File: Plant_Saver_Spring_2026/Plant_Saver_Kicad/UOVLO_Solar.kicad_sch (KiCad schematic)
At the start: 10 parts, among them Q10 G09P02L, Q11 SSF1341, U5 MCP6547T_I_MS

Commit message: Footprint correction
Changed the DHT20 from a header pin to the recommended SIP. Also had to reannotate in order to assign footprints.
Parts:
- renumbered Q11 to Q9, R34 to R38, R35 to R39, R36 to R40, R30 to R41, R31 to R42, R37 to R43, R38 to R44, U5 to U17
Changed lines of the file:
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@@
 		(dnp no)
 		(fields_autoplaced yes)
-		(property "Reference" "U5"
+		(property "Reference" "U17"
 			(at 158.75 71.12 0)
 			(effects
@@
 			(project ""
 				(path "/7f244634-d37a-4ff0-ba36-8027330ab1bd/c1b5c94f-5fb5-4e2b-895b-5d171c372d7d/9fa29de7-25a7-4316-bbea-8ab2651dedf4"
-					(reference "U5")
+					(reference "U17")
 					(unit 1)
 				)
@@
 		(dnp no)
 		(fields_autoplaced yes)
-		(property "Reference" "U5"
+		(property "Reference" "U17"
 			(at 158.75 91.44 0)
 			(effects
@@
 			(project ""
 				(path "/7f244634-d37a-4ff0-ba36-8027330ab1bd/c1b5c94f-5fb5-4e2b-895b-5d171c372d7d/9fa29de7-25a7-4316-bbea-8ab2651dedf4"
-					(reference "U5")
+					(reference "U17")
 					(unit 2)
 				)
@@
 		(dnp no)
 		(fields_autoplaced yes)
-		(property "Reference" "U5"
+		(property "Reference" "U17"
 			(at 104.14 120.65 90)
 			(effects
@@
 			(project ""
 				(path "/7f244634-d37a-4ff0-ba36-8027330ab1bd/c1b5c94f-5fb5-4e2b-895b-5d171c372d7d/9fa29de7-25a7-4316-bbea-8ab2651dedf4"
-					(reference "U5")
+					(reference "U17")
 					(unit 3)
 				)
@@
 		(dnp no)
 		(fields_autoplaced yes)
-		(property "Reference" "R35"
+		(property "Reference" "R39"
 			(at 116.84 91.4399 0)
 			(effects
@@
 			(project "Plant_Saver_Dev"
 				(path "/7f244634-d37a-4ff0-ba36-8027330ab1bd/c1b5c94f-5fb5-4e2b-895b-5d171c372d7d/9fa29de7-25a7-4316-bbea-8ab2651dedf4"
-					(reference "R35")
+					(reference "R39")
 					(unit 1)
 				)
@@
 		(dnp no)
 		(fields_autoplaced yes)
-		(property "Reference" "R30"
+		(property "Reference" "R41"
 			(at 140.97 83.8199 0)
 			(effects
@@
 			(project "Plant_Saver_Dev"
 				(path "/7f244634-d37a-4ff0-ba36-8027330ab1bd/c1b5c94f-5fb5-4e2b-895b-5d171c372d7d/9fa29de7-25a7-4316-bbea-8ab2651dedf4"
-					(reference "R30")
+					(reference "R41")
 					(unit 1)
 				)
@@
 		(dnp no)
 		(fields_autoplaced yes)
-		(property "Reference" "R38"
+		(property "Reference" "R44"
 			(at 203.2 74.93 90)
 			(effects
@@
 			(project "Plant_Saver_Dev"
 				(path "/7f244634-d37a-4ff0-ba36-8027330ab1bd/c1b5c94f-5fb5-4e2b-895b-5d171c372d7d/9fa29de7-25a7-4316-bbea-8ab2651dedf4"
-					(reference "R38")
+					(reference "R44")
 					(unit 1)
 				)
@@
 		(dnp no)
 		(fields_autoplaced yes)
-		(property "Reference" "#PWR022"
+		(property "Reference" "#PWR030"
 			(at 114.3 134.62 0)
 			(effects
@@
 			(project ""
 				(path "/7f244634-d37a-4ff0-ba36-8027330ab1bd/c1b5c94f-5fb5-4e2b-895b-5d171c372d7d/9fa29de7-25a7-4316-bbea-8ab2651dedf4"
-					(reference "#PWR022")
+					(reference "#PWR030")
 					(unit 1)
 				)
@@
 		(dnp no)
 		(fields_autoplaced yes)
-		(property "Reference" "R34"
+		(property "Reference" "R38"
 			(at 116.84 73.6599 0)
 			(effects
@@
 			(project "Plant_Saver_Dev"
 				(path "/7f244634-d37a-4ff0-ba36-8027330ab1bd/c1b5c94f-5fb5-4e2b-895b-5d171c372d7d/9fa29de7-25a7-4316-bbea-8ab2651dedf4"
-					(reference "R34")
+					(reference "R38")
 					(unit 1)
 				)
@@
 		(dnp no)
 		(fields_autoplaced yes)
-		(property "Reference" "R37"
+		(property "Reference" "R43"
 			(at 175.26 73.6599 0)
 			(effects
@@
 			(project "Plant_Saver_Dev"
 				(path "/7f244634-d37a-4ff0-ba36-8027330ab1bd/c1b5c94f-5fb5-4e2b-895b-5d171c372d7d/9fa29de7-25a7-4316-bbea-8ab2651dedf4"
-					(reference "R37")
+					(reference "R43")
 					(unit 1)
 				)
@@
 		(dnp no)
 		(fields_autoplaced yes)
-		(property "Reference" "R36"
+		(property "Reference" "R40"
 			(at 116.84 110.4899 0)
 			(effects
@@
 			(project "Plant_Saver_Dev"
 				(path "/7f244634-d37a-4ff0-ba36-8027330ab1bd/c1b5c94f-5fb5-4e2b-895b-5d171c372d7d/9fa29de7-25a7-4316-bbea-8ab2651dedf4"
-					(reference "R36")
+					(reference "R40")
 					(unit 1)
 				)
@@
 		(dnp no)
 		(fields_autoplaced yes)
-		(property "Reference" "#PWR023"
+		(property "Reference" "#PWR031"
 			(at 209.55 90.17 0)
 			(effects
@@
 			(project ""
 				(path "/7f244634-d37a-4ff0-ba36-8027330ab1bd/c1b5c94f-5fb5-4e2b-895b-5d171c372d7d/9fa29de7-25a7-4316-bbea-8ab2651dedf4"
-					(reference "#PWR023")
+					(reference "#PWR031")
 					(unit 1)
 				)
@@
 		(dnp no)
 		(fields_autoplaced yes)
-		(property "Reference" "R31"
+		(property "Reference" "R42"
 			(at 140.97 96.5199 0)
 			(effects
@@
 			(project "Plant_Saver_Dev"
 				(path "/7f244634-d37a-4ff0-ba36-8027330ab1bd/c1b5c94f-5fb5-4e2b-895b-5d171c372d7d/9fa29de7-25a7-4316-bbea-8ab2651dedf4"
-					(reference "R31")
+					(reference "R42")
 					(unit 1)
 				)
@@
 		(on_board yes)
 		(dnp no)
-		(property "Reference" "Q11"
+		(property "Reference" "Q9"
 			(at 201.93 91.44 90)
 			(effects
@@
 			(project "Plant_Saver_Dev"
 				(path "/7f244634-d37a-4ff0-ba36-8027330ab1bd/c1b5c94f-5fb5-4e2b-895b-5d171c372d7d/9fa29de7-25a7-4316-bbea-8ab2651dedf4"
-					(reference "Q11")
-					(unit 1)
-				)
+					(reference "Q9")
+					(unit 1)
+				)

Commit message: Charging updates and MicroSD started
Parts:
- R41: value 22.1K -> 205K
- R42: value 15K -> 301K
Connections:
- net GND: now also R38.2; no longer R40.2
- net Vcc: now also R40.1; no longer R38.1
- net at R39.1, U17.3 (+): now also R40.2; no longer R38.2
- net at R39.2, U17.6 (-): now also R38.1; no longer R40.1
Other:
- moved on the sheet: R38, R40
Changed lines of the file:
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@@
+	)
+	(junction
+		(at 114.3 78.74)
+		(diameter 0)
+		(color 0 0 0 0)
 	)
 	(junction
@@
 	(junction
 		(at 114.3 125.73)
-		(diameter 0)
-		(color 0 0 0 0)
-	)
-	(junction
-		(at 114.3 78.74)
 		(diameter 0)
 		(color 0 0 0 0)
@@
 			)
 		)
-		(property "Value" "22.1K"
+		(property "Value" "205K"
 			(at 140.97 86.3599 0)
 			(effects
@@
 	(symbol
 		(lib_id "Device:R_US")
-		(at 114.3 74.93 0)
+		(at 114.3 111.76 0)
 		(unit 1)
 		(exclude_from_sim no)
@@
 		(fields_autoplaced yes)
 		(property "Reference" "R38"
-			(at 116.84 73.6599 0)
+			(at 116.84 110.4899 0)
 			(effects
 				(font
@@
 		)
 		(property "Value" "402K"
-			(at 116.84 76.1999 0)
+			(at 116.84 113.0299 0)
 			(effects
 				(font
@@
 		)
 		(property "Footprint" "Resistor_THT:R_Axial_DIN0207_L6.3mm_D2.5mm_P10.16mm_Horizontal"
-			(at 115.316 75.184 90)
+			(at 115.316 112.014 90)
 			(effects
 				(font
@@
 		)
 		(property "Datasheet" "~"
-			(at 114.3 74.93 0)
+			(at 114.3 111.76 0)
 			(effects
 				(font
@@
 		)
 		(property "Description" "Resistor, US symbol"
-			(at 114.3 74.93 0)
+			(at 114.3 111.76 0)
 			(effects
 				(font
@@
 	(symbol
 		(lib_id "Device:R_US")
-		(at 114.3 111.76 0)
+		(at 114.3 74.93 0)
 		(unit 1)
 		(exclude_from_sim no)
@@
 		(fields_autoplaced yes)
 		(property "Reference" "R40"
-			(at 116.84 110.4899 0)
+			(at 116.84 73.6599 0)
 			(effects
 				(font
@@
 		)
 		(property "Value" "22.1K"
-			(at 116.84 113.0299 0)
+			(at 116.84 76.1999 0)
 			(effects
 				(font
@@
 		)
 		(property "Footprint" "Resistor_THT:R_Axial_DIN0207_L6.3mm_D2.5mm_P10.16mm_Horizontal"
-			(at 115.316 112.014 90)
+			(at 115.316 75.184 90)
 			(effects
 				(font
@@
 		)
 		(property "Datasheet" "~"
-			(at 114.3 111.76 0)
+			(at 114.3 74.93 0)
 			(effects
 				(font
@@
 		)
 		(property "Description" "Resistor, US symbol"
-			(at 114.3 111.76 0)
+			(at 114.3 74.93 0)
 			(effects
 				(font
@@
 			)
 		)
-		(property "Value" "15K"
+		(property "Value" "301K"
 			(at 140.97 99.0599 0)
 			(effects

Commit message: Misc. Charging Changes
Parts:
- removed Q9: SSF1341, Package_TO_SOT_SMD:SOT-23_Handsoldering, symbol Simulation_SPICE:PMOS
- added Q11: ISP12DP06NMXTSA1, ul_ISP12DP06NMXTSA1:PG-SOT223-4_INF, symbol Simulation_SPICE:PMOS
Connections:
- net Vin: now also Q11.3 (S)
- net at R43.2, U17.1, U17.7: now also Q11.2 (G)
- net at Q10.2 (G), R44.2: now also Q11.1 (D)
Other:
- note removed: "Double-Check This"
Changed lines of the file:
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@@
 	(generator_version "9.0")
 	(paper "A4")
-	(rectangle
-		(start 181.61 59.69)
-		(end 222.25 104.14)
-		(stroke
-			(width 0)
-			(type dash_dot)
-		)
-		(fill
-			(type none)
-		)
-	)
-	(text "Double-Check This"
-		(exclude_from_sim no)
-		(at 190.246 58.166 0)
-		(effects
-			(font
-				(size 1.27 1.27)
-			)
-		)
-	)
 	(text "Voltage window: 4.5 to 5.3 V"
 		(exclude_from_sim no)
-		(at 152.4 52.07 0)
+		(at 147.32 61.214 0)
 		(effects
 			(font
@@
 	)
 	(symbol
+		(lib_id "Simulation_SPICE:PMOS")
+		(at 193.04 91.44 0)
+		(unit 1)
+		(exclude_from_sim no)
+		(in_bom yes)
+		(on_board yes)
+		(dnp no)
+		(property "Reference" "Q11"
+			(at 201.93 91.44 90)
+			(effects
+				(font
+					(size 1.27 1.27)
+				)
+			)
+		)
+		(property "Value" "ISP12DP06NMXTSA1"
+			(at 199.39 91.44 90)
+			(effects
+				(font
+					(size 1.27 1.27)
+				)
+			)
+		)
+		(property "Footprint" "ul_ISP12DP06NMXTSA1:PG-SOT223-4_INF"
+			(at 198.12 88.9 0)
+			(effects
+				(font
+					(size 1.27 1.27)
+				)
+				(hide yes)
+			)
+		)
+		(property "Datasheet" ""
+			(at 193.04 104.14 0)
+			(effects
+				(font
+					(size 1.27 1.27)
+				)
+				(hide yes)
+			)
+		)
+		(property "Description" "P-MOSFET transistor, drain/source/gate"
+			(at 193.04 91.44 0)
+			(effects
+				(font
+					(size 1.27 1.27)
+				)
+				(hide yes)
+			)
+		)
+		(property "Sim.Device" "PMOS"
+			(at 193.04 108.585 0)
+			(effects
+				(font
+					(size 1.27 1.27)
+				)
+				(hide yes)
+			)
+		)
+		(property "Sim.Type" "VDMOS"
+			(at 193.04 110.49 0)
+			(effects
+				(font
+					(size 1.27 1.27)
+				)
+				(hide yes)
+			)
+		)
+		(property "Sim.Pins" "1=D 2=G 3=S"
+			(at 193.04 106.68 0)
+			(effects
+				(font
+					(size 1.27 1.27)
+				)
+				(hide yes)
+			)
+		)
+		(pin "1"
+		)
+		(pin "2"
+		)
+		(pin "3"
+		)
+		(instances
+			(project "Plant_Saver_Kicad"
+				(path "/7f244634-d37a-4ff0-ba36-8027330ab1bd/c1b5c94f-5fb5-4e2b-895b-5d171c372d7d/9fa29de7-25a7-4316-bbea-8ab2651dedf4"
+					(reference "Q11")
+					(unit 1)
+				)
+			)
+		)
+	)
+	(symbol
 		(lib_id "power:GND")
 		(at 209.55 83.82 0)
@@
 					(unit 1)
 				)
-			)
-		)
-	)
-	(symbol
-		(lib_id "Simulation_SPICE:PMOS")
-		(at 193.04 91.44 0)
-		(unit 1)
-		(exclude_from_sim no)
-		(in_bom yes)
-		(on_board yes)
-		(dnp no)
-		(property "Reference" "Q9"
-			(at 201.93 91.44 90)
-			(effects
-				(font
-					(size 1.27 1.27)
-				)
-			)
-		)
-		(property "Value" "SSF1341"
-			(at 199.39 91.44 90)
-			(effects
-				(font
-					(size 1.27 1.27)
-				)
-			)
-		)
-		(property "Footprint" "Package_TO_SOT_SMD:SOT-23_Handsoldering"
-			(at 198.12 88.9 0)
-			(effects
-				(font
-					(size 1.27 1.27)
-				)
-				(hide yes)
-			)
-		)
-		(property "Datasheet" "https://ngspice.sourceforge.io/docs/ngspice-html-manual/manual.xhtml#cha_MOSFETs"
-			(at 193.04 104.14 0)
-			(effects
-				(font
-					(size 1.27 1.27)
-				)
-				(hide yes)
-			)
-		)
-		(property "Description" "P-MOSFET transistor, drain/source/gate"
-			(at 193.04 91.44 0)
-			(effects
-				(font
-					(size 1.27 1.27)
-				)
-				(hide yes)
-			)
-		)
-		(property "Sim.Device" "PMOS"
-			(at 193.04 108.585 0)
-			(effects
-				(font
-					(size 1.27 1.27)
-				)
-				(hide yes)
-			)
-		)
-		(property "Sim.Type" "VDMOS"
-			(at 193.04 110.49 0)
-			(effects
-				(font
-					(size 1.27 1.27)
-				)
-				(hide yes)
-			)
-		)
-		(property "Sim.Pins" "1=D 2=G 3=S"
-			(at 193.04 106.68 0)
-			(effects
-				(font
-					(size 1.27 1.27)
-				)
-				(hide yes)
-			)
-		)
-		(pin "1"
-		)
-		(pin "2"
-		)
-		(pin "3"
-		)
-		(instances
-			(project "Plant_Saver_Dev"
-				(path "/681e180a-075d-4ade-9671-1538248e0c71/5dcd62e6-4375-4774-94ca-6833cc877f09/07016fe8-f0cf-4d61-95d5-2562fb102b33"
-					(reference "Q11")
-					(unit 1)
-				)
-			)
-			(project "Plant_Saver_Dev"
-				(path "/7f244634-d37a-4ff0-ba36-8027330ab1bd/c1b5c94f-5fb5-4e2b-895b-5d171c372d7d/9fa29de7-25a7-4316-bbea-8ab2651dedf4"
-					(reference "Q9")
-					(unit 1)
-				)

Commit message: Started PCB
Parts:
- renumbered Q10 to Q12, R40 to R37, R39 to R38, R38 to R39, R41 to R40, R42 to R41, R43 to R42, R44 to R43, U17 to U16
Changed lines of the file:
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@@
 		(dnp no)
 		(fields_autoplaced yes)
-		(property "Reference" "U17"
+		(property "Reference" "U16"
 			(at 158.75 71.12 0)
 			(effects
@@
 			(project ""
 				(path "/7f244634-d37a-4ff0-ba36-8027330ab1bd/c1b5c94f-5fb5-4e2b-895b-5d171c372d7d/9fa29de7-25a7-4316-bbea-8ab2651dedf4"
-					(reference "U17")
+					(reference "U16")
 					(unit 1)
 				)
@@
 		(dnp no)
 		(fields_autoplaced yes)
-		(property "Reference" "U17"
+		(property "Reference" "U16"
 			(at 158.75 91.44 0)
 			(effects
@@
 			(project ""
 				(path "/7f244634-d37a-4ff0-ba36-8027330ab1bd/c1b5c94f-5fb5-4e2b-895b-5d171c372d7d/9fa29de7-25a7-4316-bbea-8ab2651dedf4"
-					(reference "U17")
+					(reference "U16")
 					(unit 2)
 				)
@@
 		(dnp no)
 		(fields_autoplaced yes)
-		(property "Reference" "U17"
+		(property "Reference" "U16"
 			(at 104.14 120.65 90)
 			(effects
@@
 			(project ""
 				(path "/7f244634-d37a-4ff0-ba36-8027330ab1bd/c1b5c94f-5fb5-4e2b-895b-5d171c372d7d/9fa29de7-25a7-4316-bbea-8ab2651dedf4"
-					(reference "U17")
+					(reference "U16")
 					(unit 3)
 				)
@@
 		(dnp no)
 		(fields_autoplaced yes)
-		(property "Reference" "R39"
+		(property "Reference" "R38"
 			(at 116.84 91.4399 0)
 			(effects
@@
 			(project "Plant_Saver_Dev"
 				(path "/7f244634-d37a-4ff0-ba36-8027330ab1bd/c1b5c94f-5fb5-4e2b-895b-5d171c372d7d/9fa29de7-25a7-4316-bbea-8ab2651dedf4"
-					(reference "R39")
+					(reference "R38")
 					(unit 1)
 				)
@@
 		(dnp no)
 		(fields_autoplaced yes)
-		(property "Reference" "R41"
+		(property "Reference" "R40"
 			(at 140.97 83.8199 0)
 			(effects
@@
 			(project "Plant_Saver_Dev"
 				(path "/7f244634-d37a-4ff0-ba36-8027330ab1bd/c1b5c94f-5fb5-4e2b-895b-5d171c372d7d/9fa29de7-25a7-4316-bbea-8ab2651dedf4"
-					(reference "R41")
+					(reference "R40")
 					(unit 1)
 				)
@@
 		(on_board yes)
 		(dnp no)
-		(property "Reference" "Q10"
+		(property "Reference" "Q12"
 			(at 195.58 62.23 90)
 			(effects
@@
 			(project "Plant_Saver_Dev"
 				(path "/7f244634-d37a-4ff0-ba36-8027330ab1bd/c1b5c94f-5fb5-4e2b-895b-5d171c372d7d/9fa29de7-25a7-4316-bbea-8ab2651dedf4"
-					(reference "Q10")
+					(reference "Q12")
 					(unit 1)
 				)
@@
 		(dnp no)
 		(fields_autoplaced yes)
-		(property "Reference" "R44"
+		(property "Reference" "R43"
 			(at 203.2 74.93 90)
 			(effects
@@
 			(project "Plant_Saver_Dev"
 				(path "/7f244634-d37a-4ff0-ba36-8027330ab1bd/c1b5c94f-5fb5-4e2b-895b-5d171c372d7d/9fa29de7-25a7-4316-bbea-8ab2651dedf4"
-					(reference "R44")
+					(reference "R43")
 					(unit 1)
 				)
@@
 		(dnp no)
 		(fields_autoplaced yes)
-		(property "Reference" "#PWR030"
+		(property "Reference" "#PWR033"
 			(at 114.3 134.62 0)
 			(effects
@@
 			(project ""
 				(path "/7f244634-d37a-4ff0-ba36-8027330ab1bd/c1b5c94f-5fb5-4e2b-895b-5d171c372d7d/9fa29de7-25a7-4316-bbea-8ab2651dedf4"
-					(reference "#PWR030")
+					(reference "#PWR033")
 					(unit 1)
 				)
@@
 		(dnp no)
 		(fields_autoplaced yes)
-		(property "Reference" "R38"
+		(property "Reference" "R39"
 			(at 116.84 110.4899 0)
 			(effects
@@
 			(project "Plant_Saver_Dev"
 				(path "/7f244634-d37a-4ff0-ba36-8027330ab1bd/c1b5c94f-5fb5-4e2b-895b-5d171c372d7d/9fa29de7-25a7-4316-bbea-8ab2651dedf4"
-					(reference "R38")
+					(reference "R39")
 					(unit 1)
 				)
@@
 		(dnp no)
 		(fields_autoplaced yes)
-		(property "Reference" "R43"
+		(property "Reference" "R42"
 			(at 175.26 73.6599 0)
 			(effects
@@
 			(project "Plant_Saver_Dev"
 				(path "/7f244634-d37a-4ff0-ba36-8027330ab1bd/c1b5c94f-5fb5-4e2b-895b-5d171c372d7d/9fa29de7-25a7-4316-bbea-8ab2651dedf4"
-					(reference "R43")
+					(reference "R42")
 					(unit 1)
 				)
@@
 		(dnp no)
 		(fields_autoplaced yes)
-		(property "Reference" "R40"
+		(property "Reference" "R37"
 			(at 116.84 73.6599 0)
 			(effects
@@
 			(project "Plant_Saver_Dev"
 				(path "/7f244634-d37a-4ff0-ba36-8027330ab1bd/c1b5c94f-5fb5-4e2b-895b-5d171c372d7d/9fa29de7-25a7-4316-bbea-8ab2651dedf4"
-					(reference "R40")
+					(reference "R37")
 					(unit 1)
 				)
@@
 		(dnp no)
 		(fields_autoplaced yes)
-		(property "Reference" "#PWR031"
+		(property "Reference" "#PWR034"
 			(at 209.55 90.17 0)
 			(effects
@@
 			(project ""
 				(path "/7f244634-d37a-4ff0-ba36-8027330ab1bd/c1b5c94f-5fb5-4e2b-895b-5d171c372d7d/9fa29de7-25a7-4316-bbea-8ab2651dedf4"
-					(reference "#PWR031")
+					(reference "#PWR034")
 					(unit 1)
 				)
@@
 		(dnp no)
 		(fields_autoplaced yes)
-		(property "Reference" "R42"
+		(property "Reference" "R41"
 			(at 140.97 96.5199 0)
 			(effects
@@
 			(project "Plant_Saver_Dev"
 				(path "/7f244634-d37a-4ff0-ba36-8027330ab1bd/c1b5c94f-5fb5-4e2b-895b-5d171c372d7d/9fa29de7-25a7-4316-bbea-8ab2651dedf4"
-					(reference "R42")
-					(unit 1)
-				)
+					(reference "R41")
+					(unit 1)
+				)

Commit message: Resub from last
I forgot to save some of my changes from my last push
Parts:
- added C16: 0.1uF, Capacitor_THT:C_Disc_D4.7mm_W2.5mm_P5.00mm, symbol Device:C
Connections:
- net Vcc: now also C16.1; no longer U16.8 (V+)
- new net: C16.2, U16.8 (V+)
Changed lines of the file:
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@@
 	(wire
 		(pts
-			(xy 93.98 71.12) (xy 93.98 125.73)
+			(xy 93.98 71.12) (xy 93.98 110.49)
 		)
 		(stroke
@@
 		(pts
 			(xy 138.43 93.98) (xy 138.43 91.44)
+		)
+		(stroke
+			(width 0)
+			(type default)
+		)
+	)
+	(wire
+		(pts
+			(xy 93.98 118.11) (xy 93.98 125.73)
 		)
 		(stroke
@@
 					(unit 1)
 				)
+			)
+		)
+	)
+	(symbol
+		(lib_id "Device:C")
+		(at 93.98 114.3 0)
+		(unit 1)
+		(exclude_from_sim no)
+		(in_bom yes)
+		(on_board yes)
+		(dnp no)
+		(property "Reference" "C16"
+			(at 97.282 113.03 0)
+			(effects
+				(font
+					(size 1.27 1.27)
+				)
+				(justify left)
+			)
+		)
+		(property "Value" "0.1uF"
+			(at 97.282 115.57 0)
+			(effects
+				(font
+					(size 1.27 1.27)
+				)
+				(justify left)
+			)
+		)
+		(property "Footprint" "Capacitor_THT:C_Disc_D4.7mm_W2.5mm_P5.00mm"
+			(at 94.9452 118.11 0)
+			(effects
+				(font
+					(size 1.27 1.27)
+				)
+				(hide yes)
+			)
+		)
+		(property "Datasheet" "~"
+			(at 93.98 114.3 0)
+			(effects
+				(font
+					(size 1.27 1.27)
+				)
+				(hide yes)
+			)
+		)
+		(property "Description" "Unpolarized capacitor"
+			(at 93.98 114.3 0)
+			(effects
+				(font
+					(size 1.27 1.27)
+				)
+				(hide yes)
+			)
+		)
+		(pin "1"
+		)
+		(pin "2"
+		)
+		(instances
+			(project "Plant_Saver_Kicad"
+				(path "/7f244634-d37a-4ff0-ba36-8027330ab1bd/c1b5c94f-5fb5-4e2b-895b-5d171c372d7d/9fa29de7-25a7-4316-bbea-8ab2651dedf4"
+					(reference "C16")
+					(unit 1)
+				)

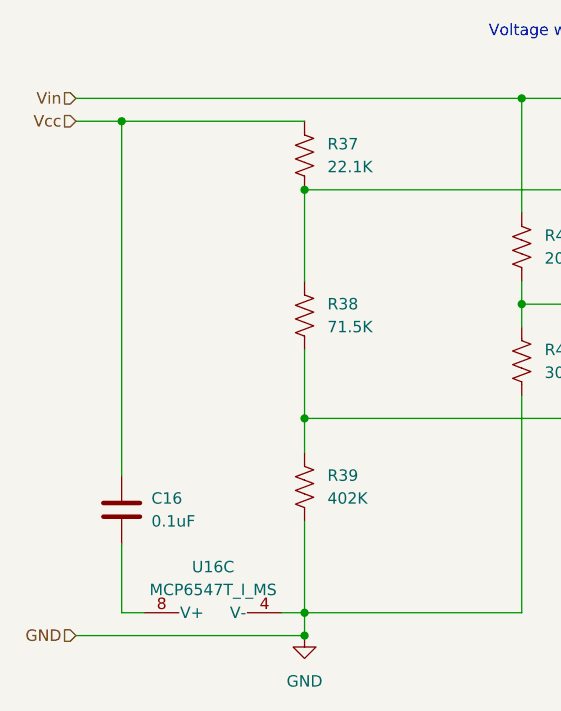
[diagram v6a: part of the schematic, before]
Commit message: Refined PCB layout
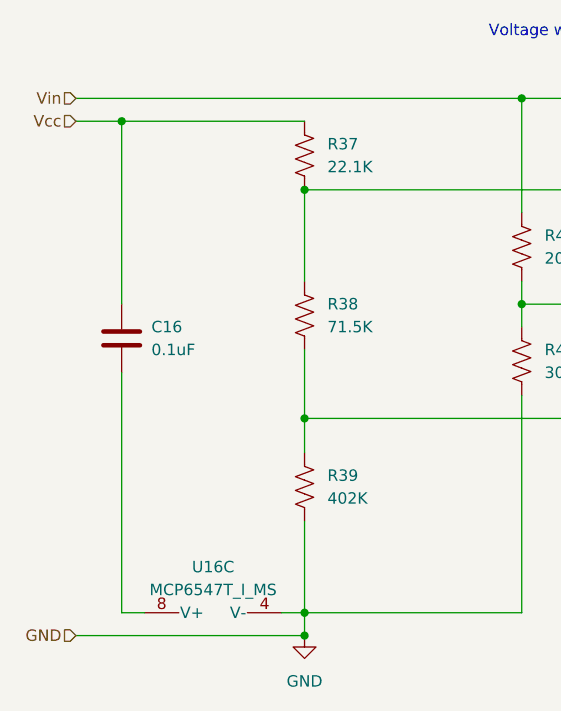
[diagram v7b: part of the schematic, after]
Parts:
- C16: footprint Capacitor_THT:C_Disc_D4.7mm_W2.5mm_P5.00mm -> Capacitor_SMD:C_1206_3216Metric_Pad1.33x1.80mm_HandSolder; Field5 (none) -> CL31A106KBHNNNE
- R42, R43: footprint Resistor_THT:R_Axial_DIN0207_L6.3mm_D2.5mm_P10.16mm_Horizontal -> Resistor_SMD:R_1206_3216Metric_Pad1.30x1.75mm_HandSolder
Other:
- moved on the sheet: C16
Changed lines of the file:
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@@
 	(wire
 		(pts
-			(xy 93.98 71.12) (xy 93.98 110.49)
+			(xy 93.98 71.12) (xy 93.98 91.44)
 		)
 		(stroke
@@
 	(wire
 		(pts
-			(xy 93.98 118.11) (xy 93.98 125.73)
+			(xy 93.98 99.06) (xy 93.98 125.73)
 		)
 		(stroke
@@
 			)
 		)
-		(property "Footprint" "Resistor_THT:R_Axial_DIN0207_L6.3mm_D2.5mm_P10.16mm_Horizontal"
+		(property "Footprint" "Resistor_SMD:R_1206_3216Metric_Pad1.30x1.75mm_HandSolder"
 			(at 202.946 82.296 90)
 			(effects
@@
 	(symbol
 		(lib_id "Device:C")
-		(at 93.98 114.3 0)
+		(at 93.98 95.25 0)
 		(unit 1)
 		(exclude_from_sim no)
@@
 		(dnp no)
 		(property "Reference" "C16"
-			(at 97.282 113.03 0)
+			(at 97.282 93.98 0)
 			(effects
 				(font
@@
 		)
 		(property "Value" "0.1uF"
-			(at 97.282 115.57 0)
+			(at 97.282 96.52 0)
 			(effects
 				(font
@@
 			)
 		)
-		(property "Footprint" "Capacitor_THT:C_Disc_D4.7mm_W2.5mm_P5.00mm"
-			(at 94.9452 118.11 0)
+		(property "Footprint" "Capacitor_SMD:C_1206_3216Metric_Pad1.33x1.80mm_HandSolder"
+			(at 94.9452 99.06 0)
 			(effects
 				(font
@@
 		)
 		(property "Datasheet" "~"
-			(at 93.98 114.3 0)
+			(at 93.98 95.25 0)
 			(effects
 				(font
@@
 		)
 		(property "Description" "Unpolarized capacitor"
-			(at 93.98 114.3 0)
+			(at 93.98 95.25 0)
+			(effects
+				(font
+					(size 1.27 1.27)
+				)
+				(hide yes)
+			)
+		)
+		(property "Field5" "CL31A106KBHNNNE"
+			(at 93.98 95.25 0)
 			(effects
 				(font
@@
 			)
 		)
-		(property "Footprint" "Resistor_THT:R_Axial_DIN0207_L6.3mm_D2.5mm_P10.16mm_Horizontal"
+		(property "Footprint" "Resistor_SMD:R_1206_3216Metric_Pad1.30x1.75mm_HandSolder"
 			(at 173.736 75.184 90)
 			(effects
